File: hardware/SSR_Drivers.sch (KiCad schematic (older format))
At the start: 23 parts, among them U10 LAA108, U11 LAA108, U4 74HC595, U5 74HC595, U6 LAA108, U7 LAA108, U8 LAA108, U9 LAA108

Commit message: Update schematic for Issue 2.
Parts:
- removed R20: 1K, Resistor_THT:R_Axial_DIN0207_L6.3mm_D2.5mm_P7.62mm_Horizontal, symbol Device:R_US
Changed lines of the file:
@@
 	1600 1400 1600 1550
-$Comp
-L Device:R_US R?
-U 1 1 5EDA0428
-P 2100 2050
-AR Path="/5EDA0428" Ref="R?"  Part="1"
-AR Path="/5EBEBADD/5EDA0428" Ref="R?"  Part="1"
-AR Path="/5EBEBADD/5ECC2A81/5EDA0428" Ref="R20"  Part="1"
-F 0 "R20" V 1895 2050 50  0000 C CNN
-F 1 "1K" V 1986 2050 50  0000 C CNN
-F 2 "Resistor_THT:R_Axial_DIN0207_L6.3mm_D2.5mm_P7.62mm_Horizontal" V 2140 2040 50  0001 C CNN
-F 3 "~" H 2100 2050 50  0001 C CNN
-	1    2100 2050
-	1    0    0    -1
-$EndComp
-Wire Wire Line
-	2100 1900 2100 1750
-Wire Wire Line
-	2100 1750 2900 1750
-Wire Wire Line
-	2900 1750 2900 2150
-Wire Wire Line
-	2900 1750 2900 1600
-Connection ~ 2900 1750
 $Comp
 L power:+5V #PWR?
@@
 	2500 2550 2000 2550
 Wire Wire Line
-	2100 2650 2100 2200
-Wire Wire Line
 	2000 2550 2000 5200
 Connection ~ 2000 5200
@@
 Wire Wire Line
 	2100 5300 2500 5300
-Connection ~ 2100 2650
 Text HLabel 1000 5200 0    50   Input ~ 0
 SSR_SRCLK
@@
 Text Notes 7150 7000 0    50   ~ 0
 (c) 2020, Howard M. Harte - WZ2Q
+Wire Wire Line
+	2900 1600 2900 2150
 $EndSCHEMATC

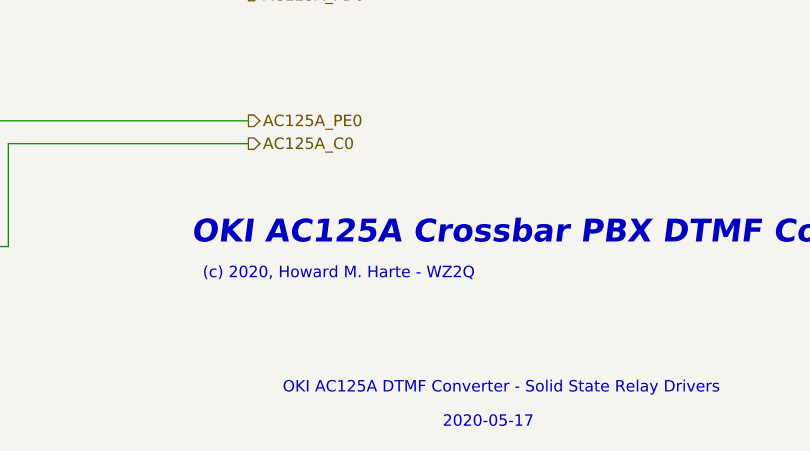
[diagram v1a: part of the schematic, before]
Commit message: Final schematic and PCB layout for Issue 2.
Corrected errors in Issue 1 and fabbed out the PCB.
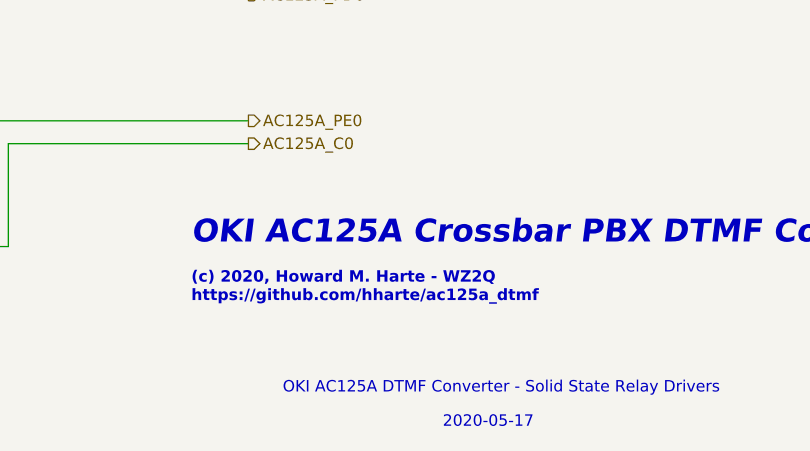
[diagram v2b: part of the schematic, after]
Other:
- note added: "(c) 2020, Howard M. Harte - WZ2Q\nhttps://github.com/hharte/ac125a_dtmf"
- note removed: "(c) 2020, Howard M. Harte - WZ2Q"
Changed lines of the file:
@@
 Text Notes 7100 6850 0    100  Italic 20
 OKI AC125A Crossbar PBX DTMF Converter
-Text Notes 7150 7000 0    50   ~ 0
-(c) 2020, Howard M. Harte - WZ2Q
 Wire Wire Line
 	2900 1600 2900 2150
+Text Notes 7100 7100 0    50   ~ 10
+(c) 2020, Howard M. Harte - WZ2Q\nhttps://github.com/hharte/ac125a_dtmf
 $EndSCHEMATC
